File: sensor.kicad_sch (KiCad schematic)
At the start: 11 parts, among them J1 Conn_01x06_Female, U2 TLV70019_SOT23-5, U3 TXB0106PWR, U4 PMW3360DM-T2QU

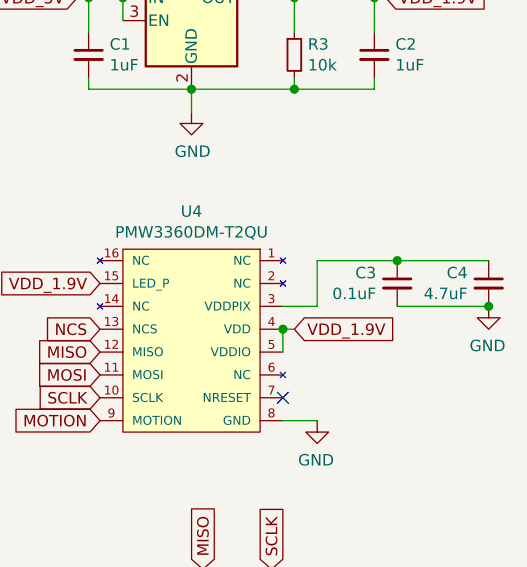
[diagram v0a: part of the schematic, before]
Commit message: add detrompeur
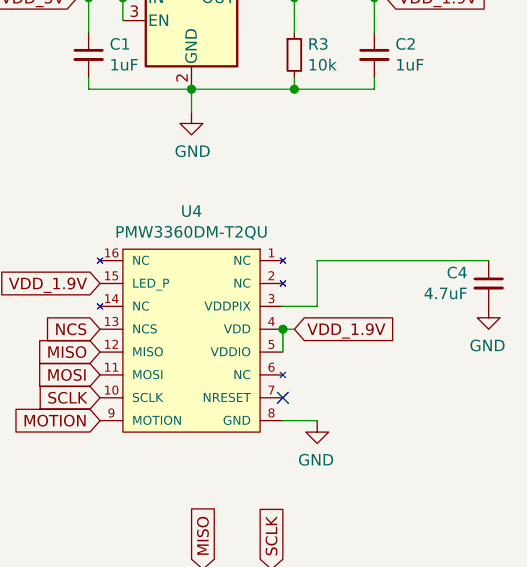
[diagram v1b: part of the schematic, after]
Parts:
- removed C3: 0.1uF, local:C_0805_2012Metric_Pad1.15x1.40mm_HandSolder, symbol Device:C_Small
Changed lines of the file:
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@@
   (junction (at 194.31 99.06) (diameter 1.016) (color 0 0 0 0))
   (junction (at 203.2 88.9) (diameter 1.016) (color 0 0 0 0))
-  (junction (at 205.74 118.11) (diameter 1.016) (color 0 0 0 0))
-  (junction (at 215.9 123.19) (diameter 1.016) (color 0 0 0 0))
   (no_connect (at 125.73 139.7))
   (no_connect (at 125.73 144.78))
@@
     (stroke (width 0) (type solid) (color 0 0 0 0))
   )
-  (wire (pts (xy 196.85 118.11) (xy 205.74 118.11))
+  (wire (pts (xy 196.85 118.11) (xy 215.9 118.11))
     (stroke (width 0) (type solid) (color 0 0 0 0))
   )
@@
   )
   (wire (pts (xy 203.2 99.06) (xy 203.2 97.79))
-    (stroke (width 0) (type solid) (color 0 0 0 0))
-  )
-  (wire (pts (xy 205.74 118.11) (xy 215.9 118.11))
-    (stroke (width 0) (type solid) (color 0 0 0 0))
-  )
-  (wire (pts (xy 205.74 123.19) (xy 215.9 123.19))
     (stroke (width 0) (type solid) (color 0 0 0 0))
   )
@@
     )
     (property "Datasheet" "~" (id 3) (at 203.2 95.25 0)
-      (effects (font (size 1.27 1.27)) hide)
-    )
-    (pin "1")
-    (pin "2")
-  )
-  (symbol (lib_id "Device:C_Small") (at 205.74 120.65 0) (mirror y) (unit 1)
-    (in_bom yes) (on_board yes)
-    (property "Reference" "C3" (id 0) (at 203.4032 119.4816 0)
-      (effects (font (size 1.27 1.27)) (justify left))
-    )
-    (property "Value" "0.1uF" (id 1) (at 203.4032 121.793 0)
-      (effects (font (size 1.27 1.27)) (justify left))
-    )
-    (property "Footprint" "local:C_0805_2012Metric_Pad1.15x1.40mm_HandSolder" (id 2) (at 205.74 120.65 0)
-      (effects (font (size 1.27 1.27)) hide)
-    )
-    (property "Datasheet" "~" (id 3) (at 205.74 120.65 0)
       (effects (font (size 1.27 1.27)) hide)
     )
@@
       (reference "C2") (unit 1) (value "1uF") (footprint "local:C_0805_2012Metric_Pad1.15x1.40mm_HandSolder")
     )
-    (path "/00000000-0000-0000-0000-00005f6c4ae0"
-      (reference "C3") (unit 1) (value "0.1uF") (footprint "local:C_0805_2012Metric_Pad1.15x1.40mm_HandSolder")
-    )
     (path "/00000000-0000-0000-0000-00005f6c443f"

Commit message: silkscreen
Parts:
- C1, C2: JLCPCB Part #（optional） (none) -> C28323; LCSC (none) -> C28323
- C4: JLCPCB Part #（optional） (none) -> C1779; LCSC (none) -> C1779
- R1, R2, R3: JLCPCB Part #（optional） (none) -> C17414; LCSC (none) -> C17414
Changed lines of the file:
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@@
+      (effects (font (size 1.27 1.27)) hide)
+    )
+    (property "JLCPCB Part #（optional）" "C17414" (id 4) (at 184.15 154.94 0)
+      (effects (font (size 1.27 1.27)) hide)
+    )
+    (property "LCSC" "C17414" (id 4) (at 184.15 154.94 0)
       (effects (font (size 1.27 1.27)) hide)
     )
@@
       (effects (font (size 1.27 1.27)) hide)
     )
+    (property "JLCPCB Part #（optional）" "C17414" (id 4) (at 191.77 154.94 0)
+      (effects (font (size 1.27 1.27)) hide)
+    )
+    (property "LCSC" "C17414" (id 4) (at 191.77 154.94 0)
+      (effects (font (size 1.27 1.27)) hide)
+    )
     (pin "1")
     (pin "2")
@@
     )
     (property "Datasheet" "~" (id 3) (at 194.31 95.25 0)
+      (effects (font (size 1.27 1.27)) hide)
+    )
+    (property "JLCPCB Part #（optional）" "C17414" (id 4) (at 194.31 95.25 0)
+      (effects (font (size 1.27 1.27)) hide)
+    )
+    (property "LCSC" "C17414" (id 4) (at 194.31 95.25 0)
       (effects (font (size 1.27 1.27)) hide)
     )
@@
       (effects (font (size 1.27 1.27)) hide)
     )
+    (property "JLCPCB Part #（optional）" "C28323" (id 4) (at 171.45 95.25 0)
+      (effects (font (size 1.27 1.27)) hide)
+    )
+    (property "LCSC" "C28323" (id 4) (at 171.45 95.25 0)
+      (effects (font (size 1.27 1.27)) hide)
+    )
     (pin "1")
     (pin "2")
@@
     )
     (property "Datasheet" "~" (id 3) (at 203.2 95.25 0)
+      (effects (font (size 1.27 1.27)) hide)
+    )
+    (property "JLCPCB Part #（optional）" "C28323" (id 4) (at 203.2 95.25 0)
+      (effects (font (size 1.27 1.27)) hide)
+    )
+    (property "LCSC" "C28323" (id 4) (at 203.2 95.25 0)
       (effects (font (size 1.27 1.27)) hide)
     )
@@
       (effects (font (size 1.27 1.27)) hide)
     )
+    (property "JLCPCB Part #（optional）" "C1779" (id 4) (at 215.9 120.65 0)
+      (effects (font (size 1.27 1.27)) hide)
+    )
+    (property "LCSC" "C1779" (id 4) (at 215.9 120.65 0)
+      (effects (font (size 1.27 1.27)) hide)
+    )
